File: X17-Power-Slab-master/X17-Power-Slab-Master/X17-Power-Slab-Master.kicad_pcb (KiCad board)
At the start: 2 copper layers, 129.5 x 119 mm, 53 parts, among them J1 61201021621, J2 ET60T-D04-3-08-D04-X-R1-S, J3 796636-6, Q2 IRF1018ESTRLPBF, SW2 1825910-6, U1 AZ1117IH-3.3TRG1, U4 STM32F091CCTx, U6 MAX485E, U7 ABLS-8.000MHZ-B2-T

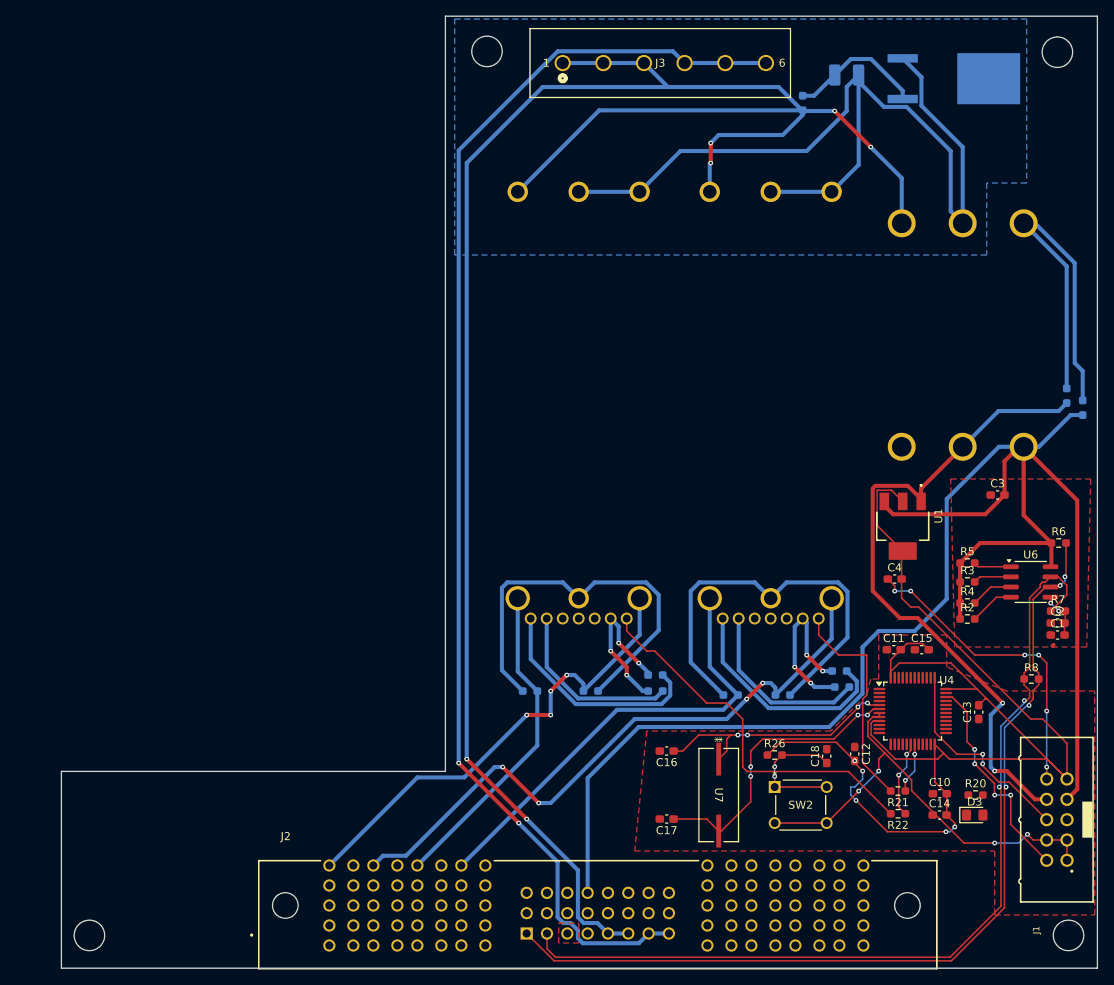
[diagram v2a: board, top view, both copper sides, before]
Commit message: Routes
Cannot fill the polygons for some reason
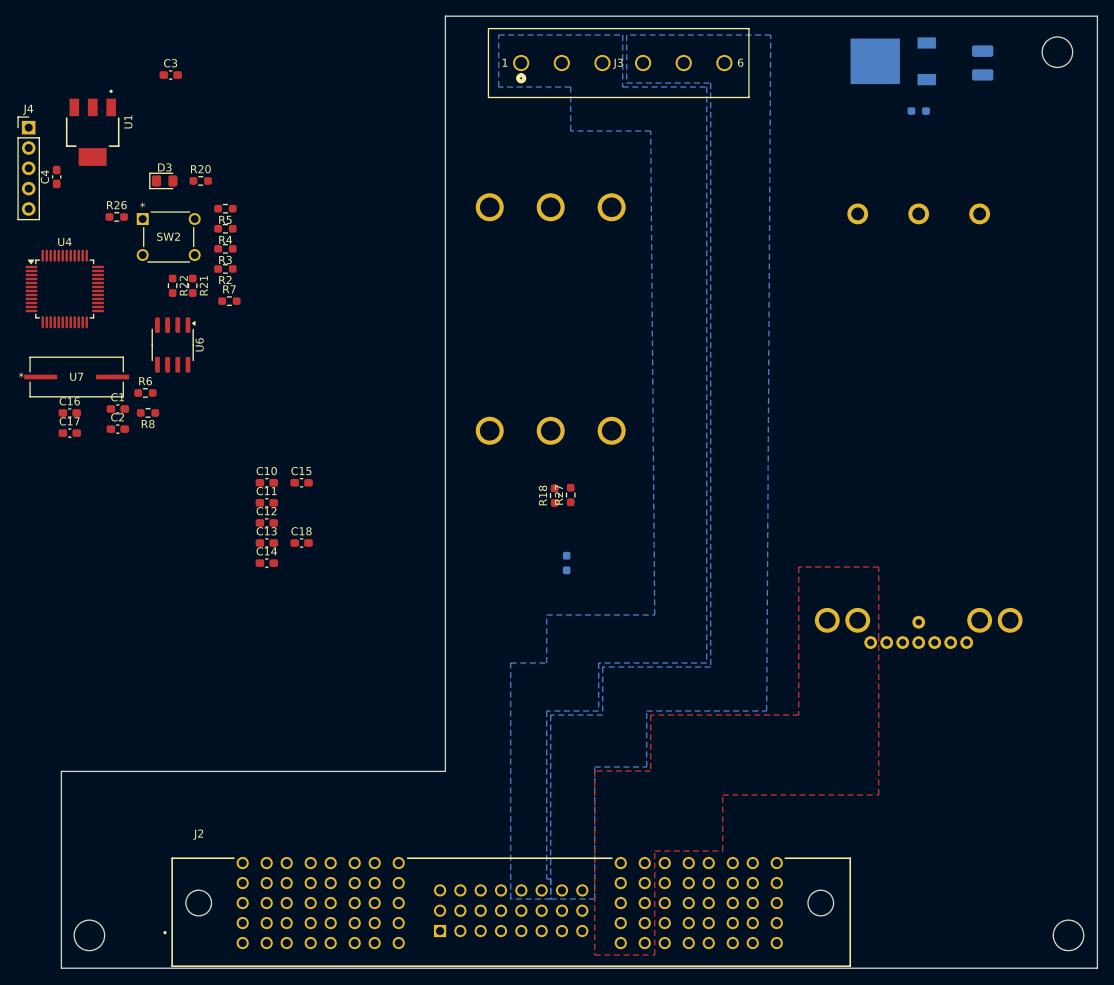
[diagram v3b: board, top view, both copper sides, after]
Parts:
- removed the H1 at (87.5, 27.0)
- removed J1: 61201021621, 612_STMconn:61201021621
- removed R11, R12, R19, R23, R24, R25, R9: 10k, Resistor_SMD:R_0603_1608Metric_Pad0.98x0.95mm_HandSolder
- removed U2, U3: ~, E48SC12030NRFH_Footprint:E48SC12030NRFH_Footprint
- added J4: Conn_01x05, Connector_PinHeader_2.54mm:PinHeader_1x05_P2.54mm_Vertical, F.Cu at (30.3, 36.6)
- added U8: ~, BMR491_MadeByMe:BMR4910203851, B.Cu at (141.5, 73.0)
- D1: value SMB8J5.0CA-E3/52 -> PZU15B3A,115
- Q2: value IRF1018ESTRLPBF -> TSM340N06CP ROG; footprint Reverse Voltage Protection:TO254P1524X483-4 -> Reverse Voltage Protection:TRANS_TSM340N06CPROG
- R1: value 10k -> 100k
- R18, R27: moved to F.Cu
- moved D3 128.6 mm to (47.3, 43.2)
- moved R20 123.6 mm to (51.8, 43.2)
- moved C1 120.8 mm to (41.4, 71.7)
- moved C2 119.9 mm to (41.4, 74.3)
- moved U4 118.4 mm to (34.8, 56.7)
- moved C4 116.2 mm to (33.8, 42.7), turned to 90 degrees
- moved C3 115.9 mm to (48.0, 30.0)
- moved R6 115.7 mm to (44.8, 69.7)
- moved R8 115.3 mm to (45.2, 72.2), turned to 180 degrees
- moved U1 112.6 mm to (38.3, 37.1)
- moved R22 112.1 mm to (48.2, 56.3), turned to -90 degrees
- moved U6 111.3 mm to (48.3, 63.7), turned to -90 degrees
- moved R7 110.6 mm to (55.3, 58.3)
- moved R21 108.5 mm to (50.8, 56.3), turned to -90 degrees
- moved R26 106.2 mm to (41.3, 47.7)
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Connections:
- C1 pad 2: NRST_PSB -> GND
- C10 pad 1: NRST_PSB -> GND
- C11 pad 1: NRST_PSB -> GND
- C12 pad 1: NRST_PSB -> GND
- C13 pad 1: NRST_PSB -> GND
- C14 pad 1: NRST_PSB -> GND
- C15 pad 1: NRST_PSB -> GND
- C16 pad 2: NRST_PSB -> GND
- C17 pad 2: NRST_PSB -> GND
- C18 pad 1: Net-(C18-Pad1) -> NRST_PSB
- C18 pad 2: NRST_PSB -> GND
- C2 pad 2: NRST_PSB -> GND
- C3 pad 1: NRST_PSB -> GND
- D3 pad 1: NRST_PSB -> GND
- J2 pad 05: 48V -> unconnected-(J2-Pad05)
- J2 pad 06: 48V -> unconnected-(J2-Pad06)
- J2 pad 07: 48V_GND -> unconnected-(J2-Pad07)
- J2 pad 08: 48V_GND -> unconnected-(J2-Pad08)
- J2 pad 19: unconnected-(J2-Pad19) -> 5V
- J2 pad 20: 5V -> 5V_GND
- J2 pad 21: 5V_GND -> 48V
- J2 pad 22: unconnected-(J2-Pad22) -> 48V
- J2 pad 23: unconnected-(J2-Pad23) -> 48V_GND
- J2 pad 24: unconnected-(J2-Pad24) -> 48V_GND
- J2 pad P01_1: 12V_GND1 -> unconnected-(J2-P01-PadP01_1)
- J2 pad P02_1: 12V_GND2 -> unconnected-(J2-P02-PadP02_1)
- J2 pad P03_1: 12V_1 -> unconnected-(J2-P03-PadP03_1)
- J2 pad P04_1: 12V_2 -> unconnected-(J2-P04-PadP04_1)
- J2 pad P05_1: unconnected-(J2-P05-PadP05_1) -> 12V
- J2 pad P08_1: unconnected-(J2-P08-PadP08_1) -> 12V_GND
- R26 pad 2: Net-(C18-Pad1) -> NRST_PSB
- R7 pad 2: NRST_PSB -> GND
- SW2 pad 1: Net-(C18-Pad1) -> NRST_PSB
- SW2 pad 2: Net-(C18-Pad1) -> NRST_PSB
- U4 pad 23: NRST_PSB -> GND
- U4 pad 35: NRST_PSB -> GND
- U4 pad 39: ALERT2 -> ALERT1
- U4 pad 44: NRST_PSB -> GND
- U4 pad 45: NRST_PSB -> GND
- U4 pad 47: NRST_PSB -> GND
- U4 pad 8: NRST_PSB -> GND
- U6 pad 5: NRST_PSB -> GND
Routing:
- net 48V_GND: track 277.2 -> 0.00 mm, vias 2 -> 0
- net 48V: track 250.1 -> 0.00 mm, vias 6 -> 0
- net 5V: track 213.4 -> 0.00 mm
- net 3.3V: track 171.6 -> 0.00 mm, vias 5 -> 0
- net 5V_GND: track 125.2 -> 0.00 mm, vias 10 -> 0
- net A+: track 114.5 -> 0.00 mm, vias 4 -> 0
- net A-: track 113.1 -> 0.00 mm, vias 2 -> 0
- net 12V_GND2: track 79.6 -> 0.00 mm, vias 4 -> 0
- net NRST_PSB: track 62.9 -> 0.00 mm, vias 6 -> 0
- net 12V_GND1: track 59.3 -> 0.00 mm, vias 4 -> 0
- net 12V_2: track 57.0 -> 0.00 mm
- net Net-(U3-TRIM): track 52.8 -> 0.00 mm
- net Net-(U2-TRIM): track 51.3 -> 0.00 mm
- net Net-(U5-Trim): track 49.8 -> 0.00 mm
- net C2_1: track 47.5 -> 0.00 mm
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- added copper zone on F.Cu, net 12V
- added copper zone on B.Cu, net 48V
- removed copper zone on F.Cu, net 3.3V_GND
- removed copper zone on F.Cu, net 5V_GND
- removed copper zone on F.Cu, net NRST_PSB

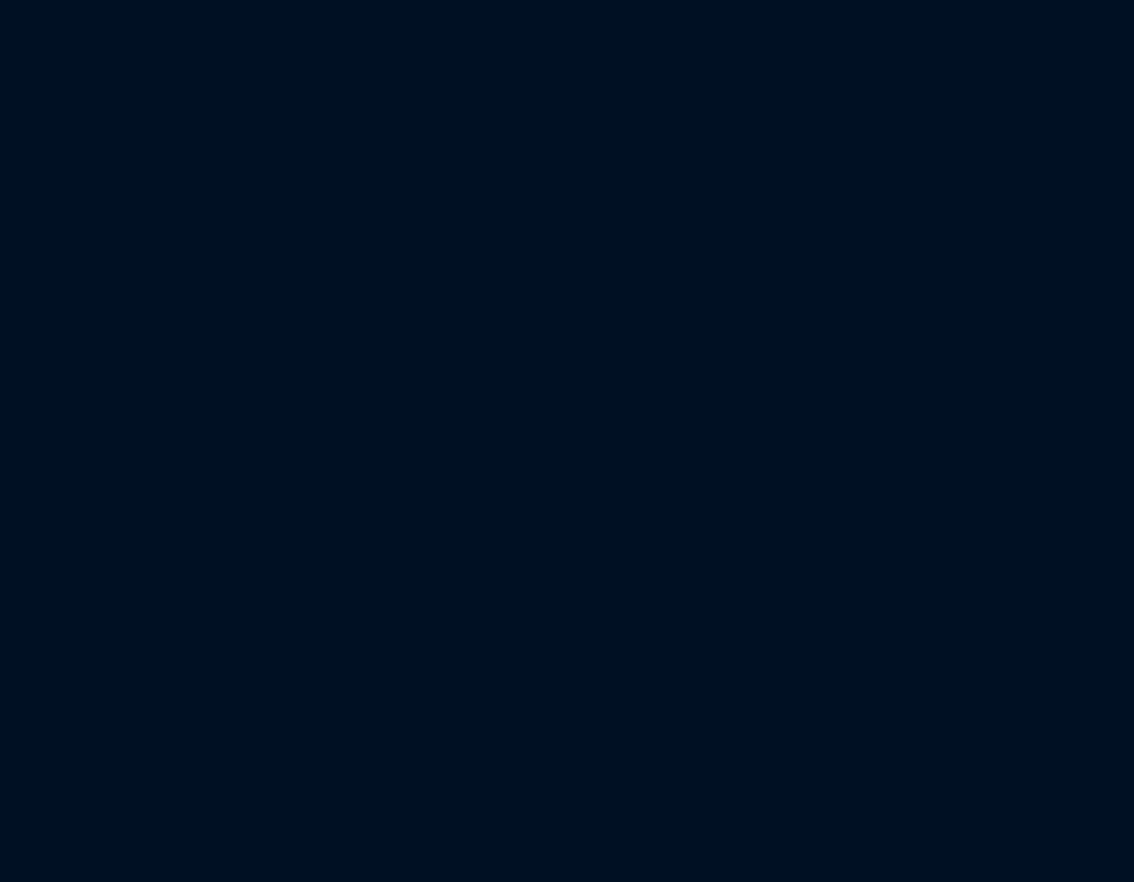
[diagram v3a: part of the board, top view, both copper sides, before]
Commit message: new dimensions
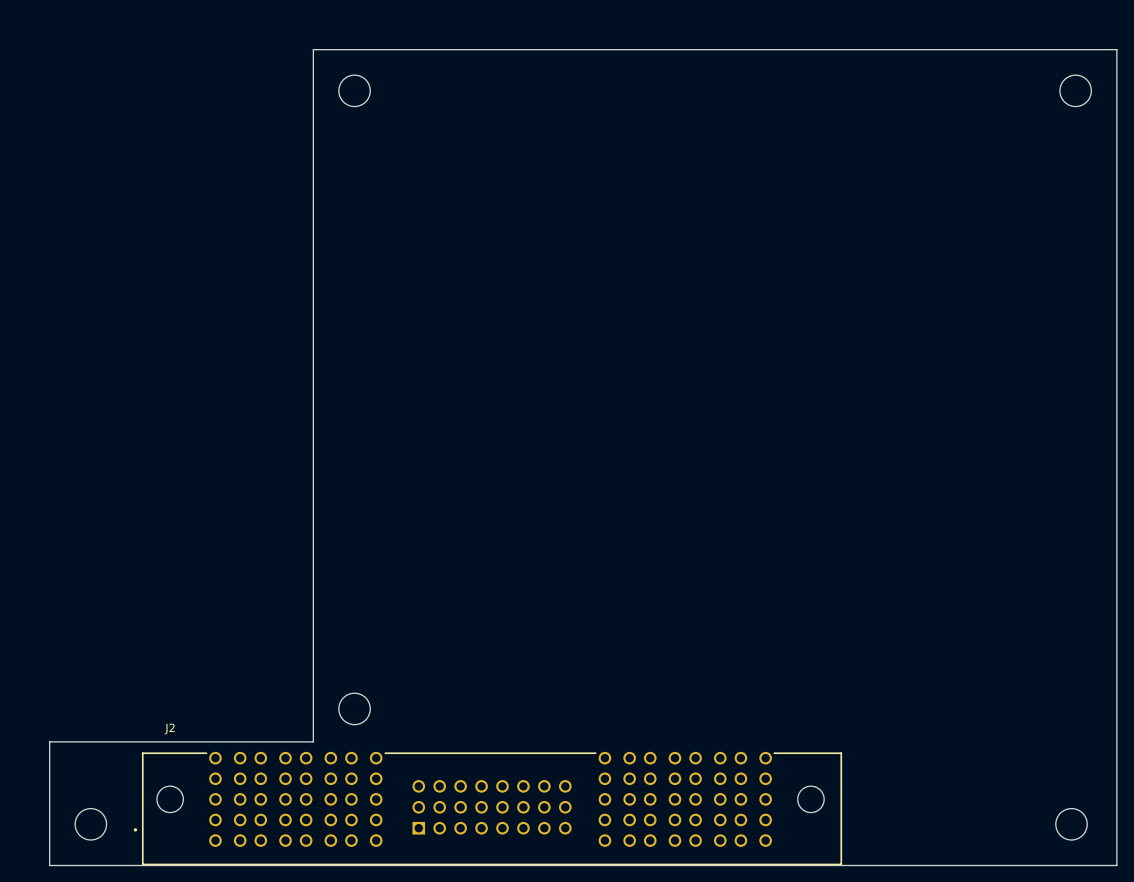
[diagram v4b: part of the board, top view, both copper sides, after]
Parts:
- added H1: 6-32-HOLE, X16_PowerSlab_V2:6-32-HOLE, B.Cu at (184.5, 138.0)
- added H1: 6-32-HOLE, X16_PowerSlab_V2:6-32-HOLE, B.Cu at (216.5, 49.0)
- added H1: 6-32-HOLE, X16_PowerSlab_V2:6-32-HOLE, B.Cu at (216.5, 124.0)
- added H3: 6-32-HOLE, X16_PowerSlab_V2:6-32-HOLE, B.Cu at (303.5, 138.0)
- added H4: 6-32-HOLE, X16_PowerSlab_V2:6-32-HOLE, B.Cu at (304.0, 49.0)
- added J2: ET60T-D04-3-08-D04-X-R1-S, ET60T-D04-3-08-D04-X-R1-S:SAMTEC_ET60T-D04-3-08-D04-X-R1-S, F.Cu at (233.0, 135.0)
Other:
- board size 129.5 x 119 mm -> 274.7 x 120.4 mm
